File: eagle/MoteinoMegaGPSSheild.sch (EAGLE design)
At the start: 24 parts, among them J1 BilgeSwitch, J2 Button, J3 LED, J4 DS18B20, J5 DS18B20, J6 5V_GND, J7 OKI-78SR-5/1.5, J8 5V, J9 12-24V_VCC, Q1 NDP6020P, Q2 IRF9Z14PBF, Q3 2N7000

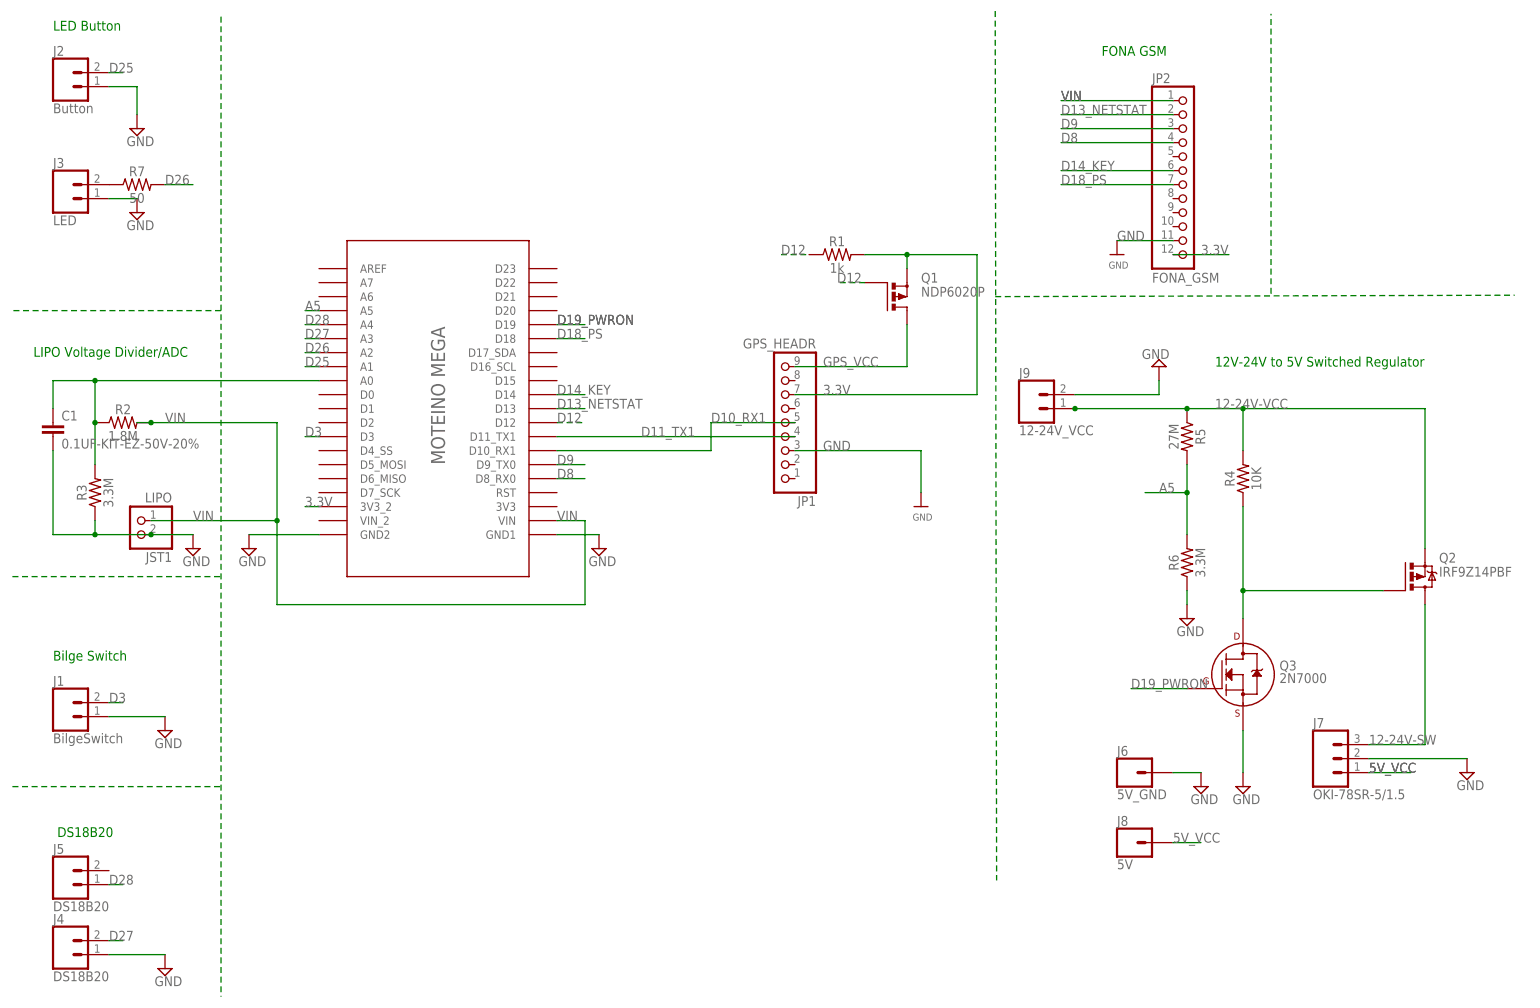
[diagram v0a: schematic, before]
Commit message: Added reverse polarity protection and fuse, as well as GSM FET
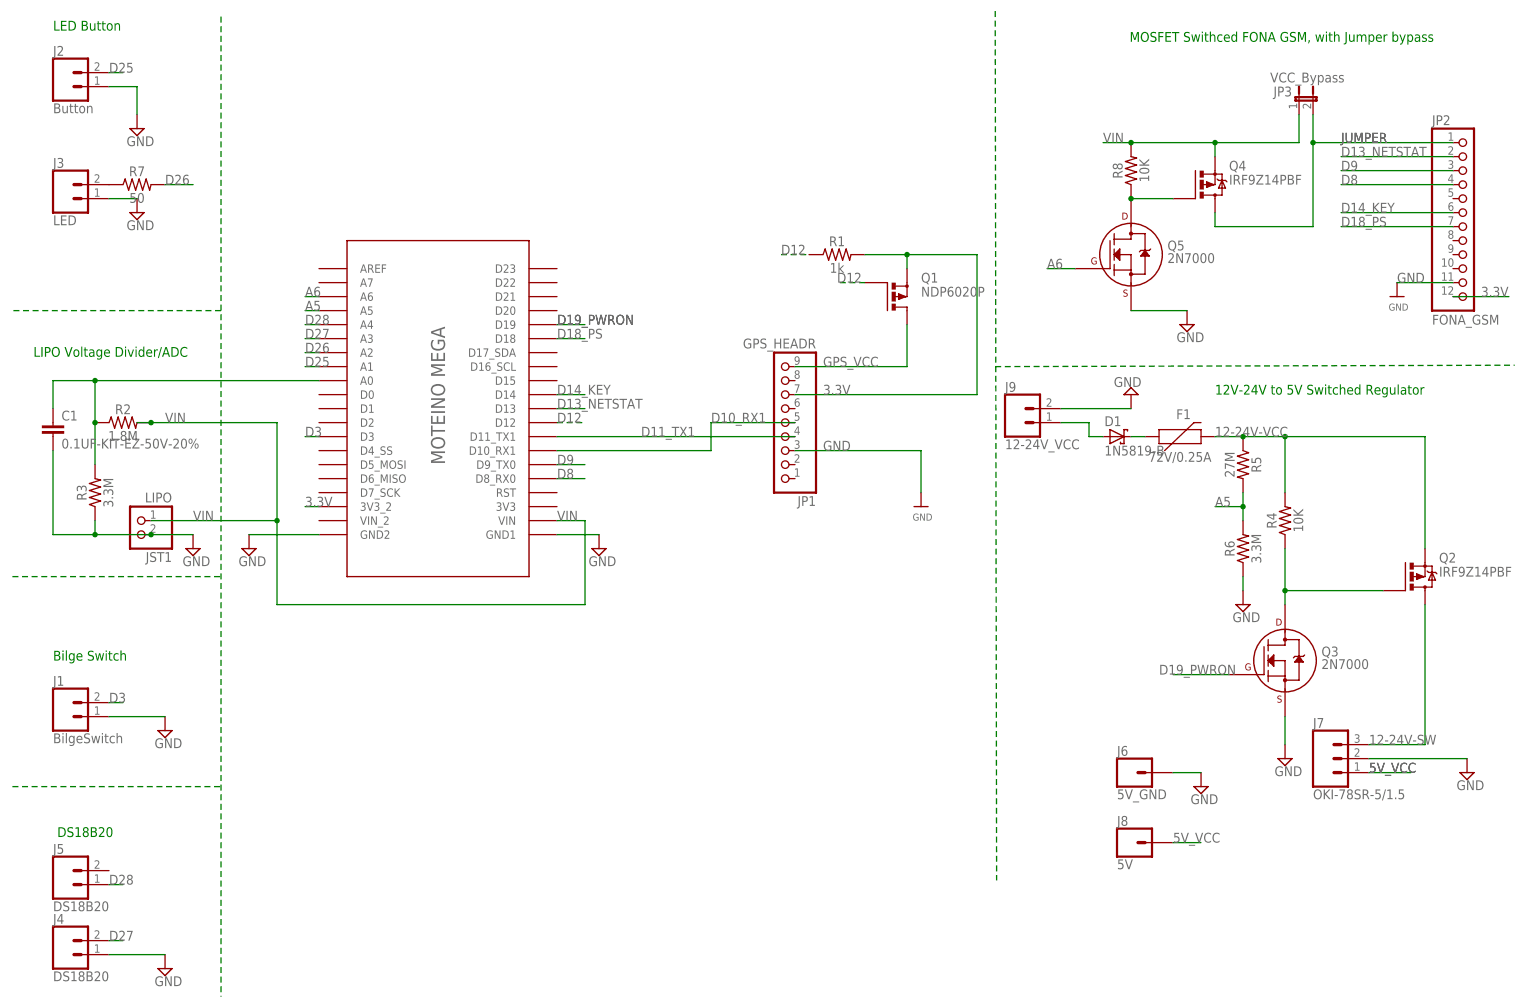
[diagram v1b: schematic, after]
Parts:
- added D1: 1N5819-B, diode:1N5819-B
- added F1: 72V/0.25A, SparkFun-Fuses:PPTC_PTH
- added JP3: VCC_Bypass, jumper:JP1E
- added Q4: IRF9Z14PBF, transistor-power:IRF9530
- added Q5: 2N7000, transistors:2N7002_TO92
- added R8: 10K, SparkFun-Resistors:1MOHM-HORIZ_KIT-1/6W-5%
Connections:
- new net A6: MOTEINO_MEGA.A6, Q5.G
- new net JUMPER: JP2.1, JP3.2, Q4.D
- new net N$5: Q4.G, Q5.D, R8.1
- new net N$6: D1.A, J9.1
- new net N$8: D1.C, F1.1
- net 12-24V-VCC: now also F1.2; no longer J9.1
- net GND: now also Q5.S
- net VIN: now also JP3.1, Q4.S, R8.2; no longer JP2.1
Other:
- note added: "MOSFET Swithced FONA GSM, with Jumper bypass"
- note removed: "FONA GSM"
- moved on the sheet: J9, JP2, Q3, R4, R5, R6

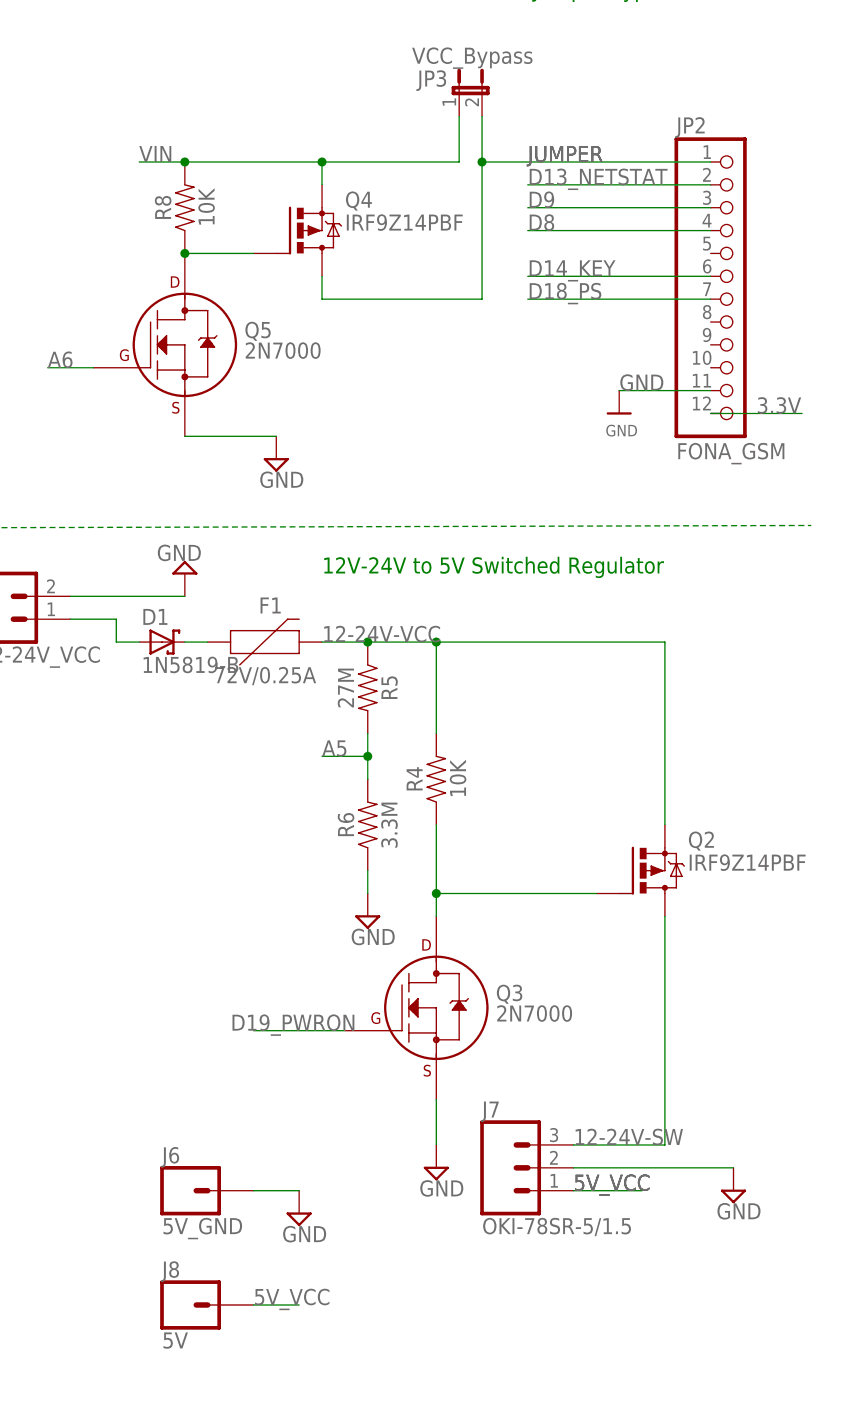
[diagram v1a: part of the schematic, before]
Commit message: Moved things around, changed P-fets
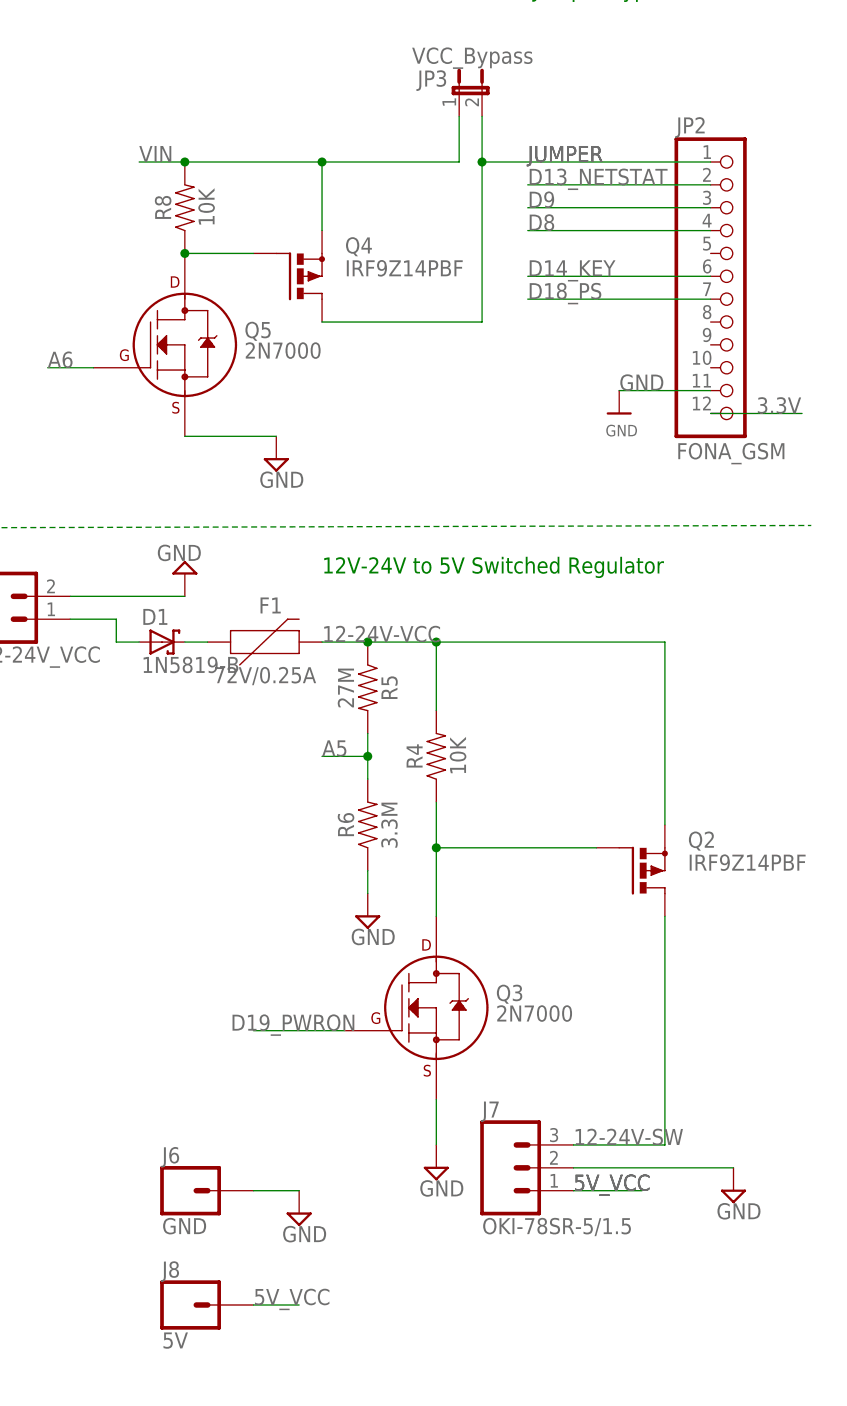
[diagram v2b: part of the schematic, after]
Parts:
- J6: value 5V_GND -> GND
- Q2, Q4: device transistor-power:IRF9530 -> transistor-power:PMOSFET_PTO220BV
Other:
- moved on the sheet: R4
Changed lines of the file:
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@@
 <attributes>
 <attribute name="CNAME" value="MoteinoMega ABoatMon Shield"/>
-<attribute name="CREVISION" value="0.99"/>
+<attribute name="CREVISION" value="0.991"/>
 <attribute name="DESIGNER" value="greg.cope@gmail.com"/>
 </attributes>
@@
 <part name="J5" library="SparkFun-Connectors" deviceset="CONN_02" device="3.5MM-NO_SILK" value="DS18B20"/>
 <part name="SUPPLY8" library="supply2" deviceset="GND" device=""/>
-<part name="Q2" library="transistor-power" deviceset="IRF9530" device="" value="IRF9Z14PBF"/>
 <part name="R4" library="SparkFun-Resistors" deviceset="1MOHM" device="-HORIZ_KIT-1/6W-5%" value="10K"/>
 <part name="Q3" library="transistors" deviceset="2N700*" device="_TO92" technology="2" value="2N7000"/>
@@
 <part name="R6" library="SparkFun-Resistors" deviceset="1MOHM" device="-HORIZ_KIT-1/6W-5%" value="3.3M"/>
 <part name="SUPPLY11" library="supply2" deviceset="GND" device=""/>
-<part name="J6" library="SparkFun-Connectors" deviceset="CONN_01" device="" value="5V_GND"/>
+<part name="J6" library="SparkFun-Connectors" deviceset="CONN_01" device="" value="GND"/>
 <part name="SUPPLY7" library="supply2" deviceset="GND" device=""/>
 <part name="J9" library="SparkFun-Connectors" deviceset="CONN_02" device="3.5MM-NO_SILK" value="12-24V_VCC"/>
@@
 <part name="C1" library="SparkFun-Capacitors" deviceset="0.1UF" device="-KIT-EZ-50V-20%" value="0.1UF-KIT-EZ-50V-20%"/>
 <part name="JP3" library="jumper" deviceset="JP1E" device="" value="VCC_Bypass"/>
-<part name="Q4" library="transistor-power" deviceset="IRF9530" device="" value="IRF9Z14PBF"/>
 <part name="Q5" library="transistors" deviceset="2N700*" device="_TO92" technology="2" value="2N7000"/>
 <part name="SUPPLY13" library="supply2" deviceset="GND" device=""/>
@@
 <part name="D1" library="diode" deviceset="1N581*" device="" technology="9-B"/>
 <part name="F1" library="SparkFun-Fuses" deviceset="PPTC" device="_PTH" value="72V/0.25A"/>
+<part name="Q2" library="transistor-power" deviceset="PMOSFET_P" device="TO220BV" value="IRF9Z14PBF"/>
+<part name="Q4" library="transistor-power" deviceset="PMOSFET_P" device="TO220BV" value="IRF9Z14PBF"/>
 </parts>
 <sheets>
@@
 <instance part="J5" gate="G$1" x="10.16" y="20.32"/>
 <instance part="SUPPLY8" gate="GND" x="27.94" y="5.08"/>
-<instance part="Q2" gate="G$1" x="254" y="76.2"/>
-<instance part="R4" gate="G$1" x="231.14" y="86.36" rot="R90"/>
+<instance part="R4" gate="G$1" x="231.14" y="88.9" rot="R90"/>
 <instance part="Q3" gate="G$1" x="231.14" y="60.96"/>
 <instance part="SUPPLY9" gate="GND" x="231.14" y="43.18"/>
@@
 <attribute name="VALUE" x="241.935" y="167.64" size="1.778" layer="96" rot="R180"/>
 </instance>
-<instance part="Q4" gate="G$1" x="215.9" y="147.32"/>
 <instance part="Q5" gate="G$1" x="203.2" y="134.62"/>
 <instance part="SUPPLY13" gate="GND" x="213.36" y="121.92"/>
@@
 <instance part="D1" gate="G$1" x="200.66" y="101.6"/>
 <instance part="F1" gate="G$1" x="210.82" y="101.6"/>
+<instance part="Q2" gate="G$1" x="254" y="76.2"/>
+<instance part="Q4" gate="G$1" x="215.9" y="142.24"/>
 </instances>
 <busses>
@@
 <label x="198.12" y="154.94" size="1.778" layer="95"/>
 <wire x1="233.68" y1="154.94" x2="218.44" y2="154.94" width="0.1524" layer="91"/>
-<pinref part="Q4" gate="G$1" pin="S"/>
 <wire x1="218.44" y1="154.94" x2="203.2" y2="154.94" width="0.1524" layer="91"/>
-<wire x1="218.44" y1="152.4" x2="218.44" y2="154.94" width="0.1524" layer="91"/>
+<wire x1="218.44" y1="147.32" x2="218.44" y2="154.94" width="0.1524" layer="91"/>
 <junction x="218.44" y="154.94"/>
 <pinref part="R8" gate="G$1" pin="2"/>
 <wire x1="203.2" y1="154.94" x2="198.12" y2="154.94" width="0.1524" layer="91"/>
 <junction x="203.2" y="154.94"/>
+<pinref part="Q4" gate="G$1" pin="S"/>
 </segment>
 </net>
@@
 <segment>
 <pinref part="R4" gate="G$1" pin="2"/>
-<wire x1="231.14" y1="91.44" x2="231.14" y2="101.6" width="0.1524" layer="91"/>
-<pinref part="Q2" gate="G$1" pin="S"/>
+<wire x1="231.14" y1="93.98" x2="231.14" y2="101.6" width="0.1524" layer="91"/>
 <wire x1="256.54" y1="81.28" x2="256.54" y2="101.6" width="0.1524" layer="91"/>
 <wire x1="256.54" y1="101.6" x2="231.14" y2="101.6" width="0.1524" layer="91"/>
@@
 <wire x1="218.44" y1="101.6" x2="223.52" y2="101.6" width="0.1524" layer="91"/>
 <junction x="223.52" y="101.6"/>
+<pinref part="Q2" gate="G$1" pin="S"/>
 </segment>
 </net>
@@
 <pinref part="Q3" gate="G$1" pin="D"/>
 <pinref part="R4" gate="G$1" pin="1"/>
-<wire x1="231.14" y1="71.12" x2="231.14" y2="73.66" width="0.1524" layer="91"/>
-<wire x1="231.14" y1="73.66" x2="231.14" y2="81.28" width="0.1524" layer="91"/>
+<wire x1="231.14" y1="71.12" x2="231.14" y2="78.74" width="0.1524" layer="91"/>
 <pinref part="Q2" gate="G$1" pin="G"/>
-<wire x1="231.14" y1="73.66" x2="248.92" y2="73.66" width="0.1524" layer="91"/>
-<junction x="231.14" y="73.66"/>
+<wire x1="231.14" y1="78.74" x2="231.14" y2="83.82" width="0.1524" layer="91"/>
+<wire x1="248.92" y1="78.74" x2="231.14" y2="78.74" width="0.1524" layer="91"/>
+<junction x="231.14" y="78.74"/>
 </segment>
 </net>
 <net name="12-24V-SW" class="1">
 <segment>
-<pinref part="Q2" gate="G$1" pin="D"/>
 <pinref part="J7" gate="J$1" pin="3"/>
 <wire x1="246.38" y1="45.72" x2="256.54" y2="45.72" width="0.1524" layer="91"/>
 <wire x1="256.54" y1="45.72" x2="256.54" y2="71.12" width="0.1524" layer="91"/>
 <label x="246.38" y="45.72" size="1.778" layer="95"/>
+<pinref part="Q2" gate="G$1" pin="D"/>
 </segment>
 </net>
@@
 <pinref part="JP3" gate="A" pin="2"/>
 <wire x1="236.22" y1="154.94" x2="236.22" y2="160.02" width="0.1524" layer="91"/>
-<wire x1="236.22" y1="154.94" x2="236.22" y2="139.7" width="0.1524" layer="91"/>
+<wire x1="236.22" y1="154.94" x2="236.22" y2="137.16" width="0.1524" layer="91"/>
 <junction x="236.22" y="154.94"/>
-<wire x1="236.22" y1="139.7" x2="218.44" y2="139.7" width="0.1524" layer="91"/>
+<wire x1="236.22" y1="137.16" x2="218.44" y2="137.16" width="0.1524" layer="91"/>
 <pinref part="Q4" gate="G$1" pin="D"/>
-<wire x1="218.44" y1="142.24" x2="218.44" y2="139.7" width="0.1524" layer="91"/>
 </segment>
 </net>
@@
 <segment>
 <pinref part="Q5" gate="G$1" pin="D"/>
-<pinref part="Q4" gate="G$1" pin="G"/>
 <wire x1="203.2" y1="144.78" x2="210.82" y2="144.78" width="0.1524" layer="91"/>
 <pinref part="R8" gate="G$1" pin="1"/>
 <junction x="203.2" y="144.78"/>
-</segment>
-</net>
+<pinref part="Q4" gate="G$1" pin="G"/>
+</segment>
+</net>
